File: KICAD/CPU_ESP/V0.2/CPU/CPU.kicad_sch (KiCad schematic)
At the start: 4 parts, among them J101 USB_B_Micro, J102 Conn_01x04, SW101 SW_Push_45deg, SW102 SW_Push_45deg

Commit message: VSCODE update
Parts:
- added J103: Conn_01x04, Connector_JST:JST_GH_SM04B-GHS-TB_1x04-1MP_P1.25mm_Horizontal, symbol Connector_Generic:Conn_01x04
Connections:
- net +5VD: now also J103.2 (Pin_2)
- net GND: now also J103.1 (Pin_1)
- net RX1: now also J103.3 (Pin_3)
- net TX1: now also J103.4 (Pin_4)
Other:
- note added: "I2C EXTERN"
- note added: "UART COMMAND"
- note added: "UART PROG/DEBUG"

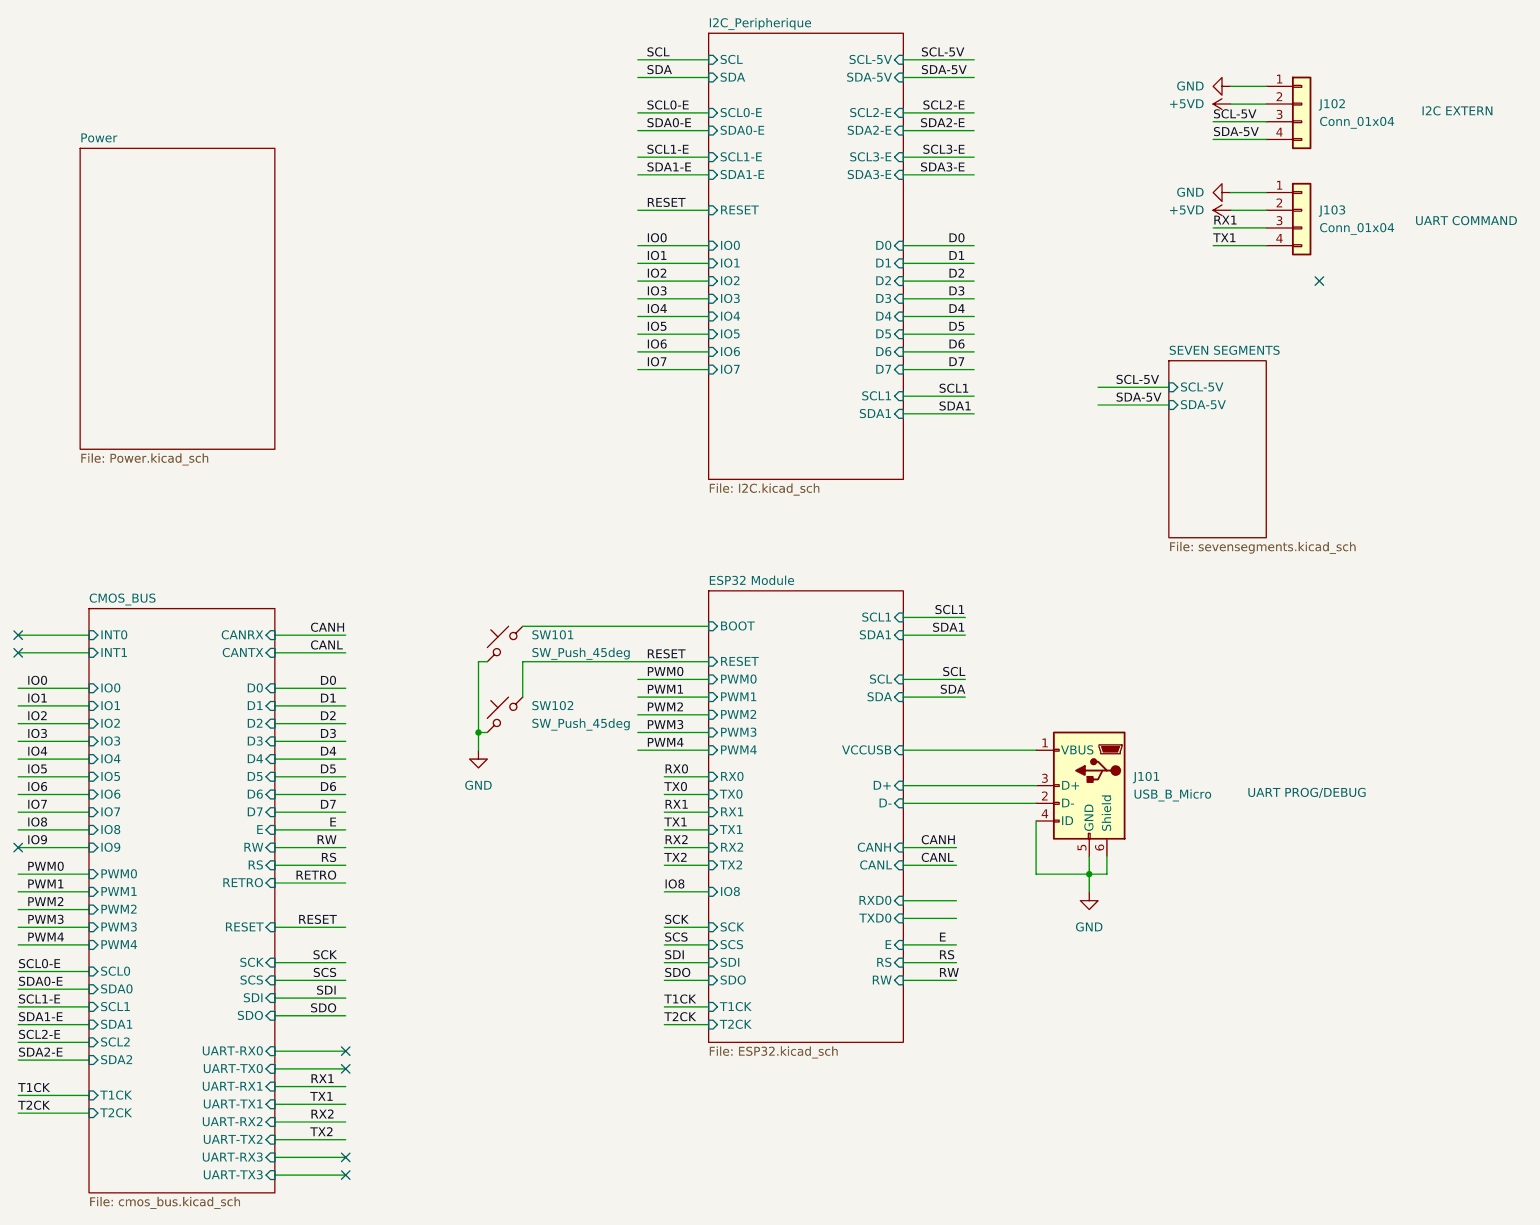
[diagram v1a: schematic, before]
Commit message: KICAD 4 UART update
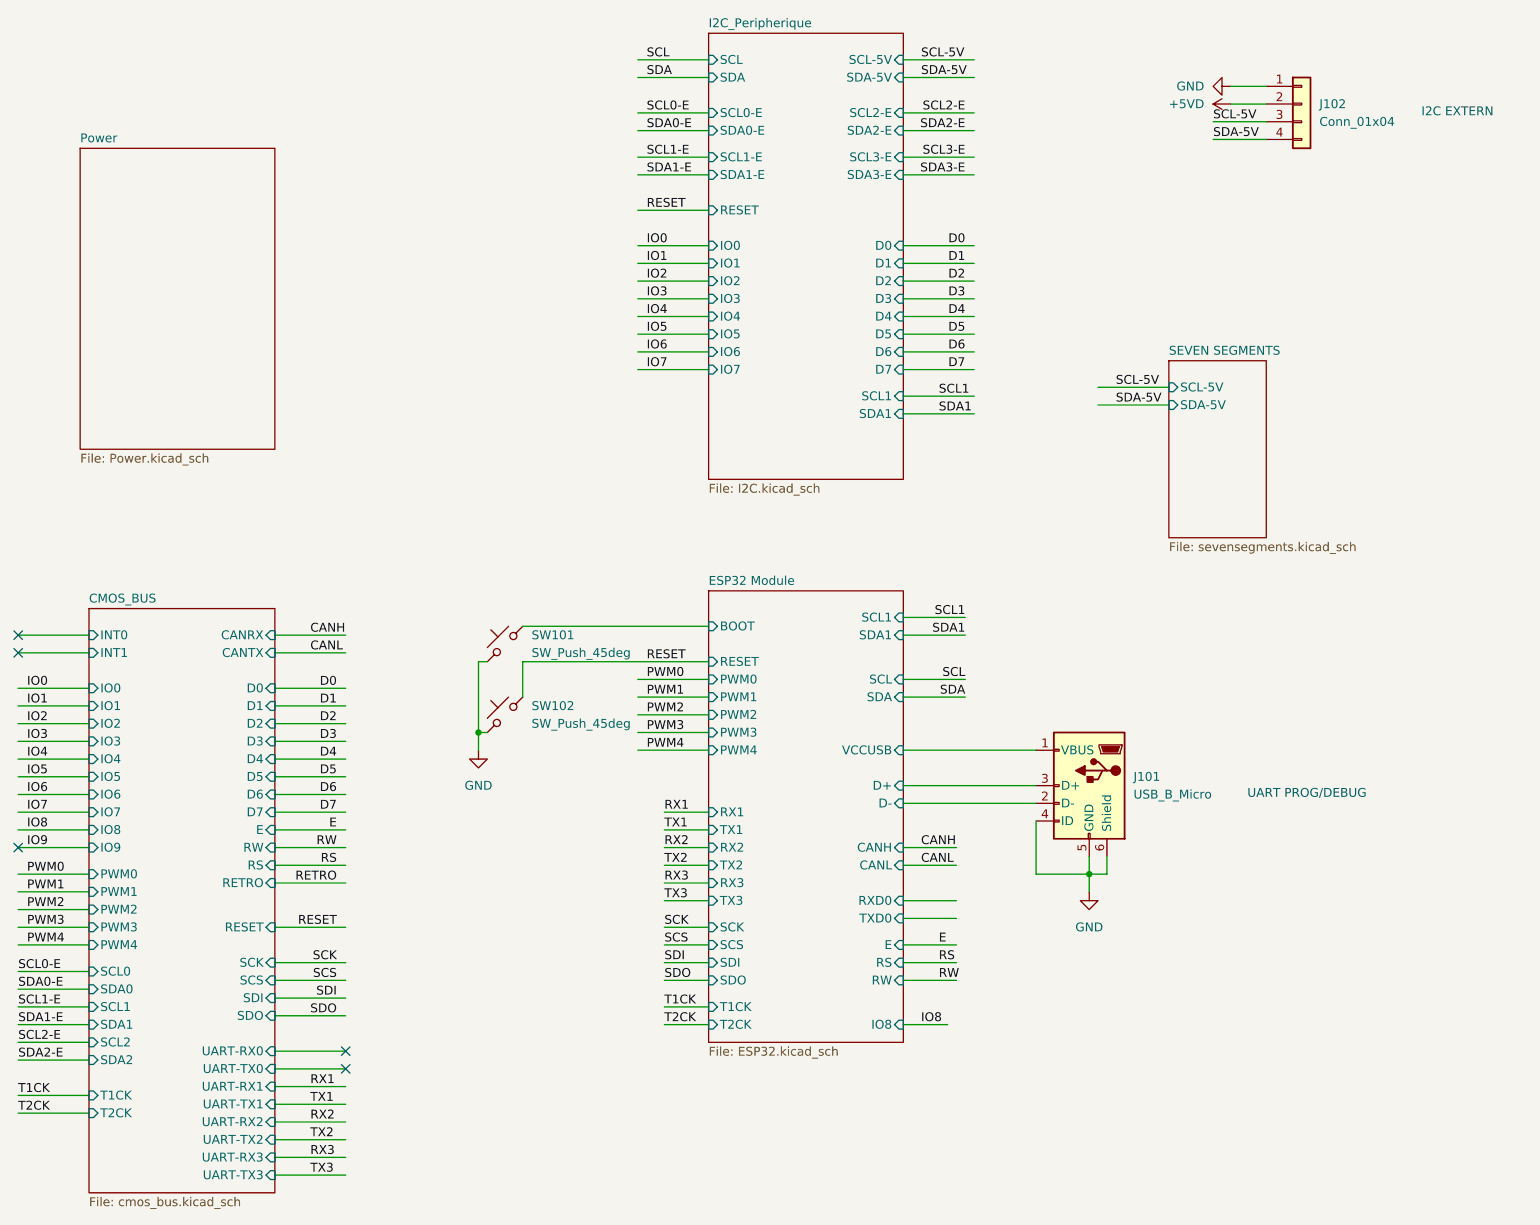
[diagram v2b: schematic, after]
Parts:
- removed J103: Conn_01x04, Connector_JST:JST_GH_SM04B-GHS-TB_1x04-1MP_P1.25mm_Horizontal, symbol Connector_Generic:Conn_01x04
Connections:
- no-connect marks 8 -> 5
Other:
- sheet ESP32 Module ports: added RX3, TX3; removed RX0, TX0
- note removed: "UART COMMAND"
